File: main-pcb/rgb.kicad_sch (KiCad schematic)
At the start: 18 parts, among them U26 74LVC1T45, U33 19-C47/RSGHBHC-5V01/2T, U34 19-C47/RSGHBHC-5V01/2T, U35 19-C47/RSGHBHC-5V01/2T, U36 19-C47/RSGHBHC-5V01/2T, U37 19-C47/RSGHBHC-5V01/2T, U38 19-C47/RSGHBHC-5V01/2T

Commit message: Under 400 unrouted
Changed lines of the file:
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@@
 	(text "1V2 IO"
 		(exclude_from_sim no)
-		(at 186.69 88.138 0)
+		(at 72.136 87.122 0)
 		(effects
 			(font
@@
 	(text "2V5 IO"
 		(exclude_from_sim no)
-		(at 110.49 88.138 0)
+		(at 148.082 87.884 0)
 		(effects
 			(font
@@
 	(text "1V8 IO"
 		(exclude_from_sim no)
-		(at 148.59 88.138 0)
+		(at 110.236 87.122 0)
 		(effects
 			(font
@@
 	(text "3V3 IO"
 		(exclude_from_sim no)
-		(at 72.39 88.138 0)
+		(at 186.436 88.646 0)
 		(effects
 			(font

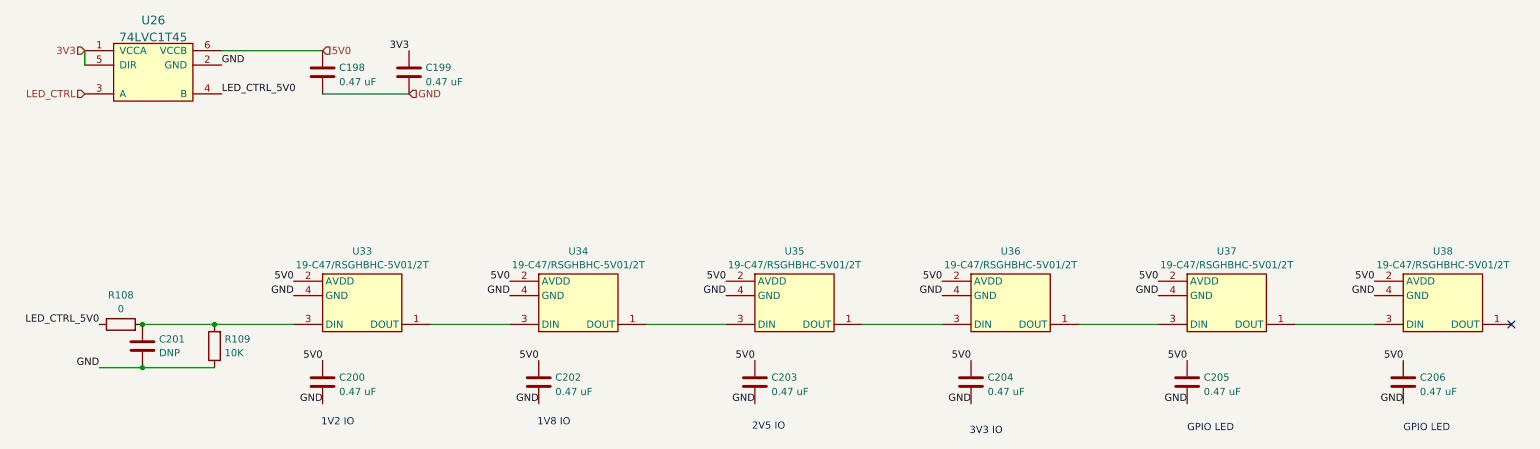
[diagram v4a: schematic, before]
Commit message: Continued routing RGMII PHY
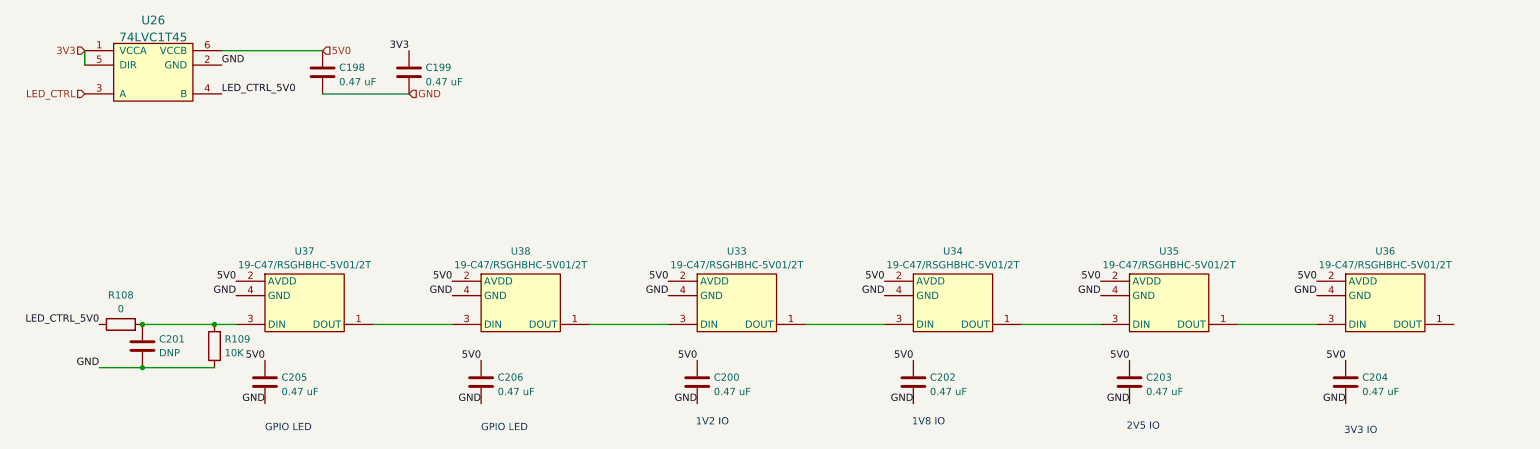
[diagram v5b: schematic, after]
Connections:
- net at C201.1, R108.2, R109.2: now also U37.3 (DIN); no longer U33.3 (DIN)
- net at U36.1 (DOUT): no longer U37.3 (DIN)
- net at U38.1 (DOUT): now also U33.3 (DIN)
- no-connect marks 1 -> 0
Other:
- moved on the sheet: C200, C202, C203, C204, C205, C206, U33, U34, U35, U36, U37, U38
